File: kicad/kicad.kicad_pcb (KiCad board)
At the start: 2 copper layers, 141 x 47 mm, 11 parts, among them J1 Screw_Terminal_01x14, U1 Pico

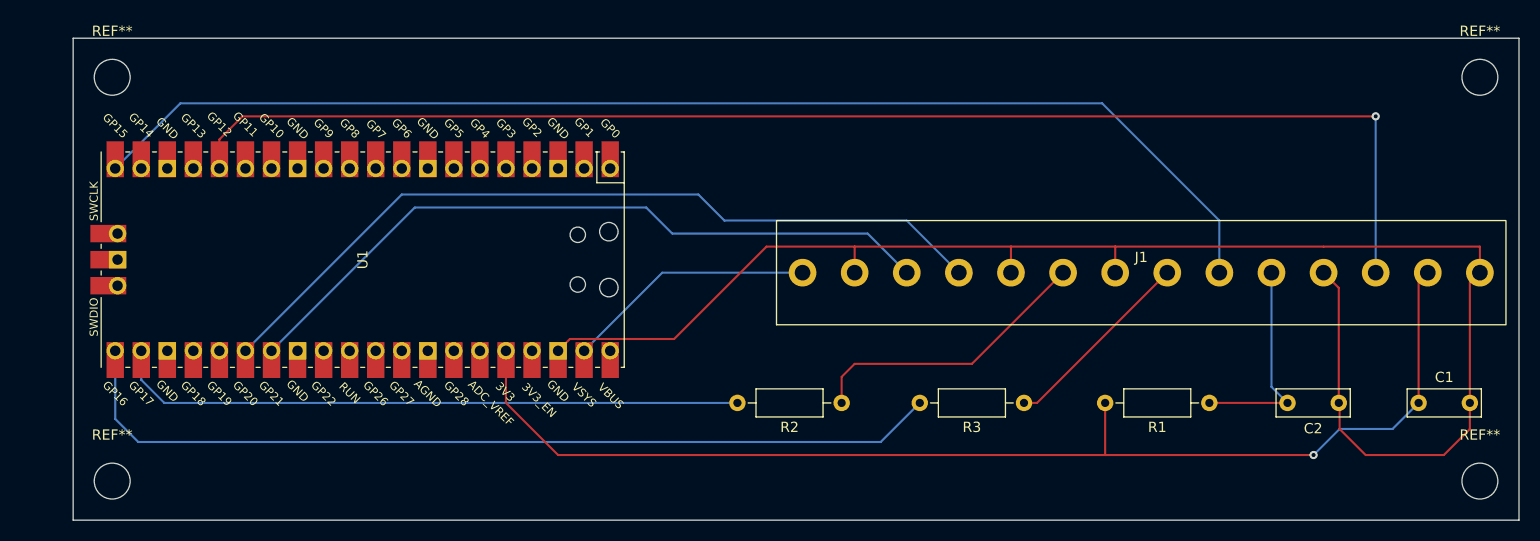
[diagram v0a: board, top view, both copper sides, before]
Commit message: new PCB layout
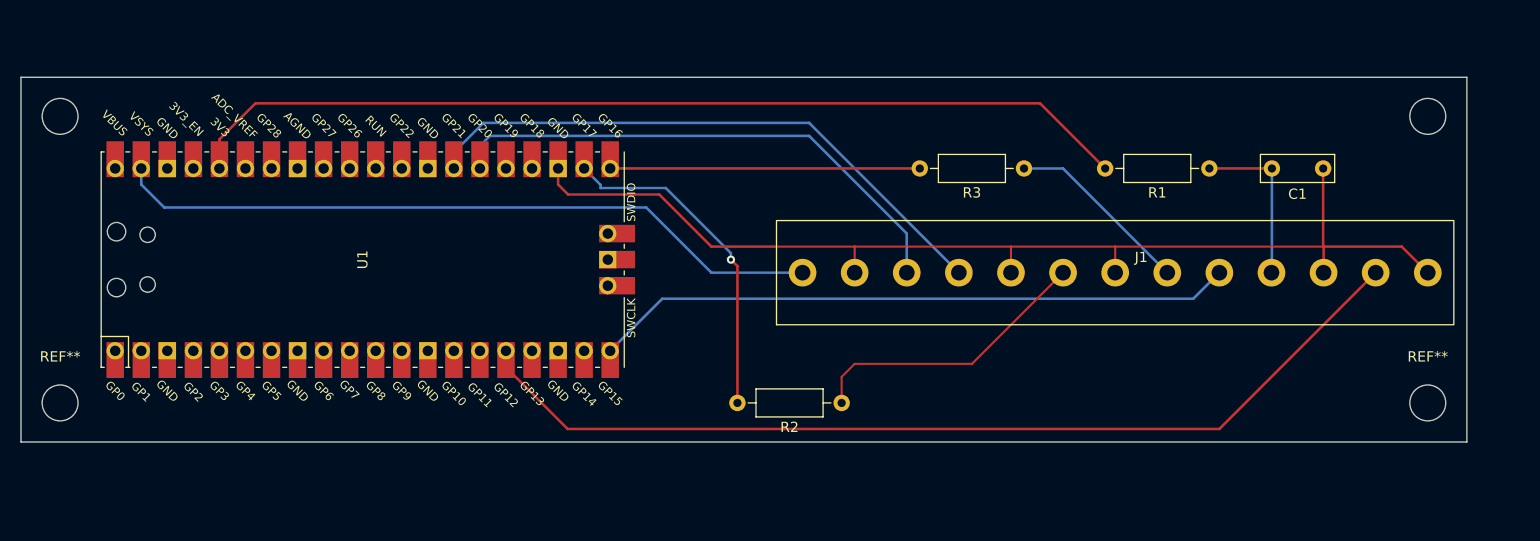
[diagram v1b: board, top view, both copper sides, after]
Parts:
- removed the C1 at (204.8, 81.3)
- J1: value Screw_Terminal_01x14 -> Screw_Terminal_01x13
- moved C1 22.9 mm to (195.5, 58.4)
- moved R1 22.9 mm to (184.4, 58.4)
- moved R3 22.9 mm to (166.4, 58.4)
- moved REF** 9.16 mm to (72.4, 81.3)
- moved REF** 9.16 mm to (205.7, 81.3)
- moved REF** 6.35 mm to (72.4, 53.3)
- moved REF** 6.35 mm to (205.7, 53.3)
- turned U1 to 90 degrees
- renumbered C2 to C1
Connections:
- J1 pad 13: Net-(J1-Pin_13) -> Net-(J1-Pin_11)
- R1 pad 2: Net-(J1-Pin_13) -> Net-(U1-3V3)
- U1 pad 23: unconnected-(U1-GND-Pad23) -> Net-(J1-Pin_11)
- U1 pad 26: Net-(J1-Pin_4) -> Net-(J1-Pin_3)
- U1 pad 27: Net-(J1-Pin_3) -> Net-(J1-Pin_4)
- U1 pad 36: Net-(J1-Pin_13) -> Net-(U1-3V3)
- U1 pad 38: Net-(J1-Pin_11) -> unconnected-(U1-GND-Pad38)
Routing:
- net Net-(J1-Pin_13): track 116.4 -> 0.00 mm, vias 1 -> 0
- net Net-(U1-3V3): track 0.00 -> 93.3 mm
- net Net-(J1-Pin_9): track 120.1 -> 62.6 mm
- net Net-(U1-GPIO16): track 87.6 -> 30.2 mm
- net Net-(J1-Pin_1): track 24.7 -> 69.6 mm
- net Net-(J1-Pin_11): track 150.6 -> 109.0 mm
- net Net-(J1-Pin_12): track 131.7 -> 95.2 mm, vias 1 -> 0
- net Net-(U1-GPIO17): track 63.5 -> 32.8 mm, vias 0 -> 1
- net Net-(J1-Pin_3): track 70.4 -> 53.6 mm
- net Net-(J1-Pin_4): track 79.0 -> 65.2 mm
- net Net-(J1-Pin_10): track 21.0 -> 16.3 mm
- net unconnected-(U1-GPIO11-Pad15): track 1.56 -> 0.00 mm
- net Net-(J1-Pin_8): track 19.2 -> 18.2 mm
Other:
- board size 141 x 47 mm -> 141 x 35.6 mm

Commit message: final kicad
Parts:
- added REF**: SOIC-8-1EP_3.9x4.9mm_P1.27mm_EP2.29x3mm, Package_SO:SOIC-8-1EP_3.9x4.9mm_P1.27mm_EP2.29x3mm, F.Cu at (170.2, 78.7)
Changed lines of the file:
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@@
       (net 2 "Net-(J1-Pin_11)") (pinfunction "Pin_13") (pintype "passive"))
+  )
+  (footprint "Package_SO:SOIC-8-1EP_3.9x4.9mm_P1.27mm_EP2.29x3mm" (layer "F.Cu")
+    (at 170.245 78.74)
+    (descr "SOIC, 8 Pin (https://www.analog.com/media/en/technical-documentation/data-sheets/ada4898-1_4898-2.pdf#page=29), generated with kicad-footprint-generator ipc_gullwing_generator.py")
+    (tags "SOIC SO")
+    (attr smd)
+    (fp_text reference "REF**" (at 0 -3.4) (layer "F.SilkS")
+        (effects (font (size 1 1) (thickness 0.15)))
+    )
+    (fp_text value "SOIC-8-1EP_3.9x4.9mm_P1.27mm_EP2.29x3mm" (at 0 3.4) (layer "F.Fab")
+        (effects (font (size 1 1) (thickness 0.15)))
+    )
+    (fp_text user "${REFERENCE}" (at 0 0) (layer "F.Fab")
+        (effects (font (size 0.98 0.98) (thickness 0.15)))
+    )
+    (fp_line (start 0 -2.56) (end -3.45 -2.56)
+      (stroke (width 0.12) (type solid)) (layer "F.SilkS"))
+    (fp_line (start 0 -2.56) (end 1.95 -2.56)
+      (stroke (width 0.12) (type solid)) (layer "F.SilkS"))
+    (fp_line (start 0 2.56) (end -1.95 2.56)
+      (stroke (width 0.12) (type solid)) (layer "F.SilkS"))
+    (fp_line (start 0 2.56) (end 1.95 2.56)
+      (stroke (width 0.12) (type solid)) (layer "F.SilkS"))
+    (fp_line (start -3.7 -2.7) (end -3.7 2.7)
+      (stroke (width 0.05) (type solid)) (layer "F.CrtYd"))
+    (fp_line (start -3.7 2.7) (end 3.7 2.7)
+      (stroke (width 0.05) (type solid)) (layer "F.CrtYd"))
+    (fp_line (start 3.7 -2.7) (end -3.7 -2.7)
+      (stroke (width 0.05) (type solid)) (layer "F.CrtYd"))
+    (fp_line (start 3.7 2.7) (end 3.7 -2.7)
+      (stroke (width 0.05) (type solid)) (layer "F.CrtYd"))
+    (fp_line (start -1.95 -1.475) (end -0.975 -2.45)
+      (stroke (width 0.1) (type solid)) (layer "F.Fab"))
+    (fp_line (start -1.95 2.45) (end -1.95 -1.475)
+      (stroke (width 0.1) (type solid)) (layer "F.Fab"))
+    (fp_line (start -0.975 -2.45) (end 1.95 -2.45)
+      (stroke (width 0.1) (type solid)) (layer "F.Fab"))
+    (fp_line (start 1.95 -2.45) (end 1.95 2.45)
+      (stroke (width 0.1) (type solid)) (layer "F.Fab"))
+    (fp_line (start 1.95 2.45) (end -1.95 2.45)
+      (stroke (width 0.1) (type solid)) (layer "F.Fab"))
+    (pad "" smd roundrect (at -0.57 -0.75) (size 0.92 1.21) (layers "F.Paste") (roundrect_rratio 0.25))
+    (pad "" smd roundrect (at -0.57 0.75) (size 0.92 1.21) (layers "F.Paste") (roundrect_rratio 0.25))
+    (pad "" smd roundrect (at 0.57 -0.75) (size 0.92 1.21) (layers "F.Paste") (roundrect_rratio 0.25))
+    (pad "" smd roundrect (at 0.57 0.75) (size 0.92 1.21) (layers "F.Paste") (roundrect_rratio 0.25))
+    (pad "1" smd roundrect (at -2.475 -1.905) (size 1.95 0.6) (layers "F.Cu" "F.Paste" "F.Mask") (roundrect_rratio 0.25))
+    (pad "2" smd roundrect (at -2.475 -0.635) (size 1.95 0.6) (layers "F.Cu" "F.Paste" "F.Mask") (roundrect_rratio 0.25))
+    (pad "3" smd roundrect (at -2.475 0.635) (size 1.95 0.6) (layers "F.Cu" "F.Paste" "F.Mask") (roundrect_rratio 0.25))
+    (pad "4" smd roundrect (at -2.475 1.905) (size 1.95 0.6) (layers "F.Cu" "F.Paste" "F.Mask") (roundrect_rratio 0.25))
+    (pad "5" smd roundrect (at 2.475 1.905) (size 1.95 0.6) (layers "F.Cu" "F.Paste" "F.Mask") (roundrect_rratio 0.25))
+    (pad "6" smd roundrect (at 2.475 0.635) (size 1.95 0.6) (layers "F.Cu" "F.Paste" "F.Mask") (roundrect_rratio 0.25))
+    (pad "7" smd roundrect (at 2.475 -0.635) (size 1.95 0.6) (layers "F.Cu" "F.Paste" "F.Mask") (roundrect_rratio 0.25))
+    (pad "8" smd roundrect (at 2.475 -1.905) (size 1.95 0.6) (layers "F.Cu" "F.Paste" "F.Mask") (roundrect_rratio 0.25))
+    (pad "9" smd rect (at 0 0) (size 2.29 3) (layers "F.Cu" "F.Mask"))
+    (model "${KICAD6_3DMODEL_DIR}/Package_SO.3dshapes/SOIC-8-1EP_3.9x4.9mm_P1.27mm_EP2.29x3mm.wrl"
+      (offset (xyz 0 0 0))
+      (scale (xyz 1 1 1))
+      (rotate (xyz 0 0 0))
+    )
   )
   (footprint "MountingHole:MountingHole_3.5mm" (layer "F.Cu")

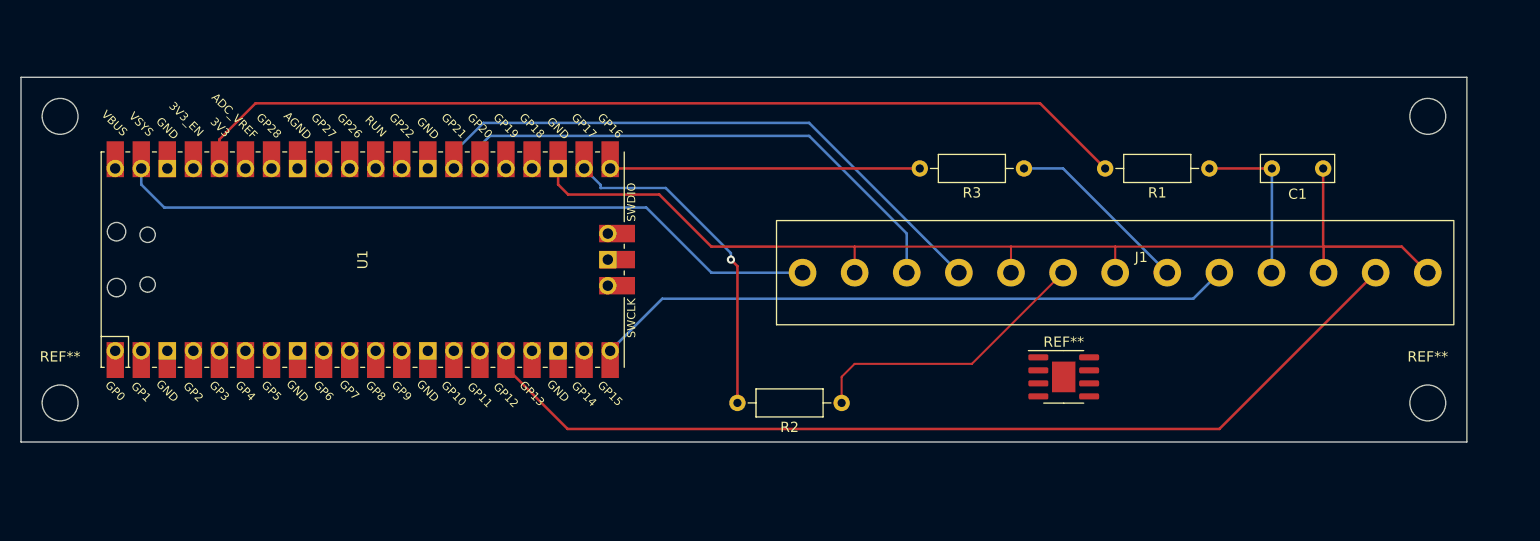
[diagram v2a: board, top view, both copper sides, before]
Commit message: add external pullup resistor
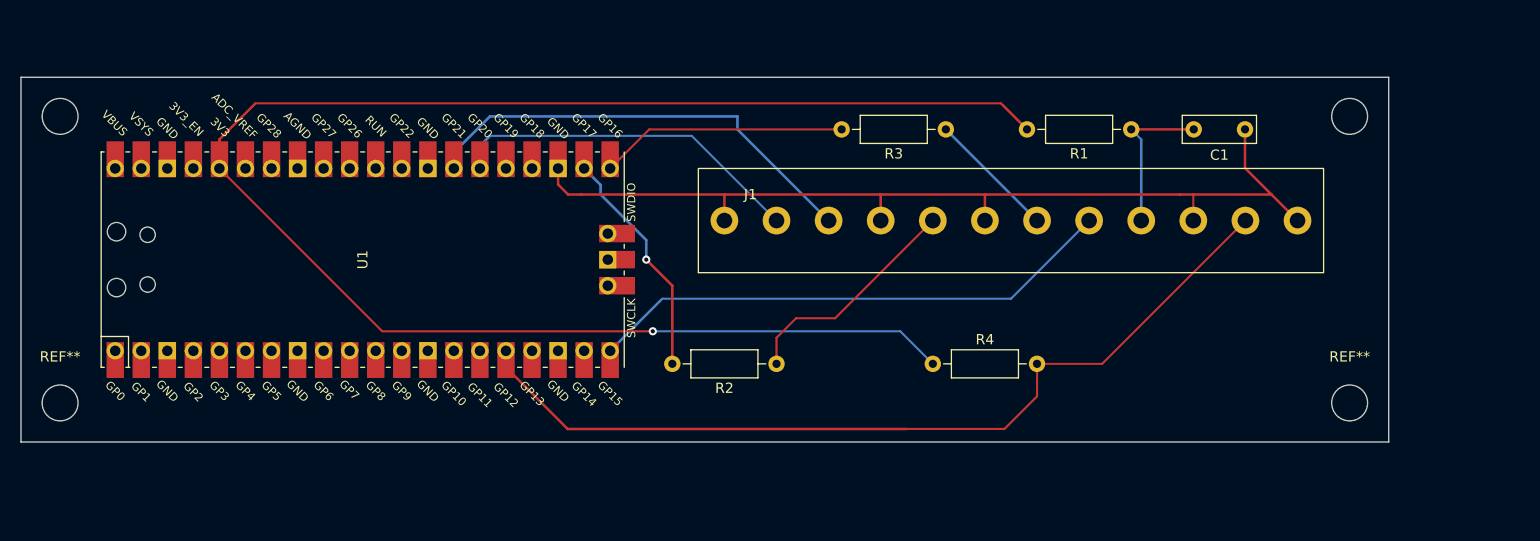
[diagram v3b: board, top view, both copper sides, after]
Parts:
- removed the REF** at (170.2, 78.7)
- added R4: 2.2kΩ, Resistor_THT:R_Axial_DIN0207_L6.3mm_D2.5mm_P10.16mm_Horizontal, F.Cu at (157.5, 77.5)
- J1: value Screw_Terminal_01x13 -> Screw_Terminal_01x12; footprint Library:terminal_block_14 -> Library:terminal_block_12
- moved J1 9.16 mm to (170.2, 66.0)
- moved C1 8.52 mm to (187.9, 54.6)
- moved R3 8.52 mm to (158.8, 54.6)
- moved R1 8.52 mm to (176.8, 54.6)
- moved REF** 7.62 mm to (198.1, 81.3)
- moved REF** 7.62 mm to (198.1, 53.3)
- moved R2 7.41 mm to (142.2, 77.5)
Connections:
- C1 pad 1: Net-(J1-Pin_11) -> Net-(J1-Pin_1)
- C1 pad 2: Net-(J1-Pin_10) -> Net-(J1-Pin_9)
- J1 pad 10: Net-(J1-Pin_10) -> Net-(J1-Pin_1)
- J1 pad 12: Net-(J1-Pin_12) -> Net-(J1-Pin_1)
- J1 pad 2: Net-(J1-Pin_11) -> Net-(J1-Pin_2)
- J1 pad 4: Net-(J1-Pin_4) -> Net-(J1-Pin_1)
- J1 pad 5: Net-(J1-Pin_11) -> Net-(J1-Pin_5)
- J1 pad 6: Net-(J1-Pin_6) -> Net-(J1-Pin_1)
- J1 pad 7: Net-(J1-Pin_11) -> Net-(J1-Pin_7)
- R1 pad 1: Net-(J1-Pin_10) -> Net-(J1-Pin_9)
- R2 pad 1: Net-(J1-Pin_6) -> Net-(J1-Pin_5)
- R3 pad 1: Net-(J1-Pin_8) -> Net-(J1-Pin_7)
- U1 pad 16: Net-(J1-Pin_12) -> Net-(J1-Pin_11)
- U1 pad 20: Net-(J1-Pin_9) -> Net-(J1-Pin_8)
- U1 pad 23: Net-(J1-Pin_11) -> Net-(J1-Pin_1)
- U1 pad 26: Net-(J1-Pin_3) -> Net-(J1-Pin_2)
- U1 pad 27: Net-(J1-Pin_4) -> Net-(J1-Pin_3)
- U1 pad 39: Net-(J1-Pin_1) -> unconnected-(U1-VSYS-Pad39)
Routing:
- net Net-(J1-Pin_12): track 95.2 -> 0.00 mm
- net Net-(U1-3V3): track 93.3 -> 161.5 mm, vias 0 -> 1
- net Net-(J1-Pin_4): track 65.2 -> 0.00 mm
- net Net-(J1-Pin_9): track 62.6 -> 15.4 mm
- net Net-(J1-Pin_2): track 0.00 -> 36.5 mm
- net Net-(J1-Pin_8): track 18.2 -> 52.0 mm
- net Net-(J1-Pin_6): track 28.3 -> 0.00 mm
- net Net-(J1-Pin_1): track 69.6 -> 92.7 mm
- net Net-(J1-Pin_5): track 0.00 -> 22.5 mm
- net Net-(J1-Pin_11): track 109.0 -> 86.5 mm
- net Net-(J1-Pin_10): track 16.3 -> 0.00 mm
- net Net-(J1-Pin_7): track 0.00 -> 12.6 mm
- net Net-(U1-GPIO17): track 32.8 -> 22.6 mm
- net Net-(J1-Pin_3): track 53.6 -> 44.5 mm
- net Net-(U1-GPIO16): track 30.2 -> 24.1 mm
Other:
- board size 141 x 35.6 mm -> 133.4 x 35.6 mm
